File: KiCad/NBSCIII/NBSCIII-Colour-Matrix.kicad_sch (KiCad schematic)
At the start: 24 parts, among them U9 LM324

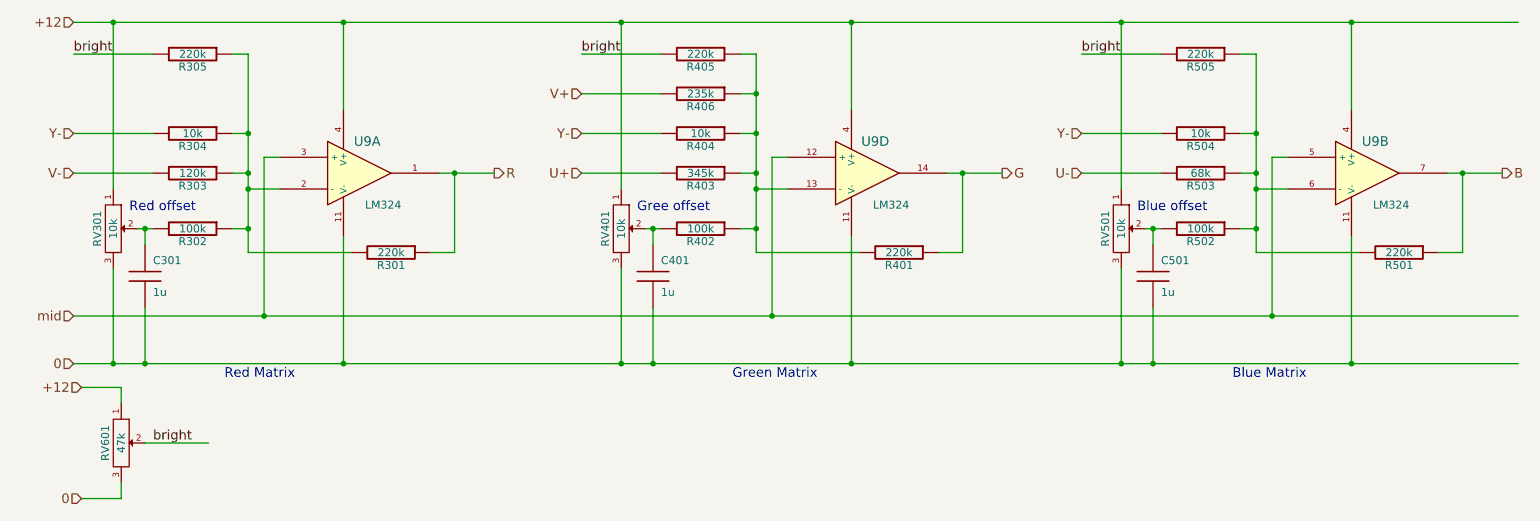
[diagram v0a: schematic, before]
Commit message: unrescue to Device:C
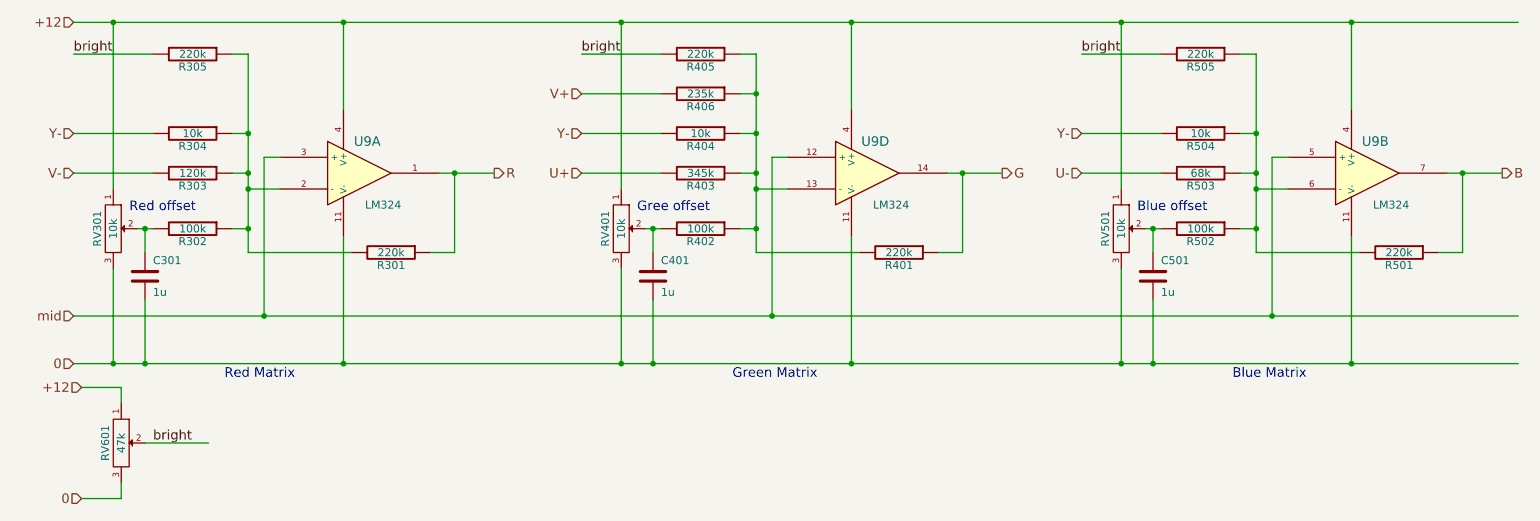
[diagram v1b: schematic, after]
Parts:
- C301, C401, C501: symbol NBSCIII-rescue:C -> Device:C
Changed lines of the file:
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@@
     (stroke (width 0) (type default) (color 0 0 0 0))
   )
-  (wire (pts (xy 123.19 82.55) (xy 123.19 91.44))
+  (wire (pts (xy 123.19 81.28) (xy 123.19 91.44))
     (stroke (width 0) (type default) (color 0 0 0 0))
   )
@@
     (stroke (width 0) (type default) (color 0 0 0 0))
   )
-  (wire (pts (xy 41.91 69.85) (xy 41.91 72.39))
+  (wire (pts (xy 41.91 69.85) (xy 41.91 73.66))
     (stroke (width 0) (type default) (color 0 0 0 0))
   )
@@
     (stroke (width 0) (type default) (color 0 0 0 0))
   )
-  (wire (pts (xy 203.2 69.85) (xy 203.2 72.39))
+  (wire (pts (xy 203.2 69.85) (xy 203.2 73.66))
     (stroke (width 0) (type default) (color 0 0 0 0))
   )
@@
     (stroke (width 0) (type default) (color 0 0 0 0))
   )
-  (wire (pts (xy 203.2 82.55) (xy 203.2 91.44))
-    (stroke (width 0) (type default) (color 0 0 0 0))
-  )
-  (wire (pts (xy 123.19 69.85) (xy 123.19 72.39))
+  (wire (pts (xy 203.2 81.28) (xy 203.2 91.44))
     (stroke (width 0) (type default) (color 0 0 0 0))
   )
@@
     (stroke (width 0) (type default) (color 0 0 0 0))
   )
+  (wire (pts (xy 123.19 69.85) (xy 123.19 73.66))
+    (stroke (width 0) (type default) (color 0 0 0 0))
+  )
   (wire (pts (xy 203.2 91.44) (xy 198.12 91.44))
     (stroke (width 0) (type default) (color 0 0 0 0))
@@
     (stroke (width 0) (type default) (color 0 0 0 0))
   )
-  (wire (pts (xy 41.91 82.55) (xy 41.91 91.44))
+  (wire (pts (xy 41.91 81.28) (xy 41.91 91.44))
     (stroke (width 0) (type default) (color 0 0 0 0))
   )
@@
     (pin "3")
   )
-  (symbol (lib_id "NBSCIII-rescue:C") (at 41.91 77.47 0) (unit 1)
+  (symbol (lib_id "Device:C") (at 41.91 77.47 0) (unit 1)
     (in_bom yes) (on_board yes)
     (property "Reference" "C301" (id 0) (at 43.18 74.93 0)
@@
     (pin "3")
   )
-  (symbol (lib_id "NBSCIII-rescue:C") (at 123.19 77.47 0) (unit 1)
+  (symbol (lib_id "Device:C") (at 123.19 77.47 0) (unit 1)
     (in_bom yes) (on_board yes)
     (property "Reference" "C401" (id 0) (at 124.46 74.93 0)
@@
     (pin "3")
   )
-  (symbol (lib_id "NBSCIII-rescue:C") (at 203.2 77.47 0) (unit 1)
+  (symbol (lib_id "Device:C") (at 203.2 77.47 0) (unit 1)
     (in_bom yes) (on_board yes)
     (property "Reference" "C501" (id 0) (at 204.47 74.93 0)

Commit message: unrescue Device:R
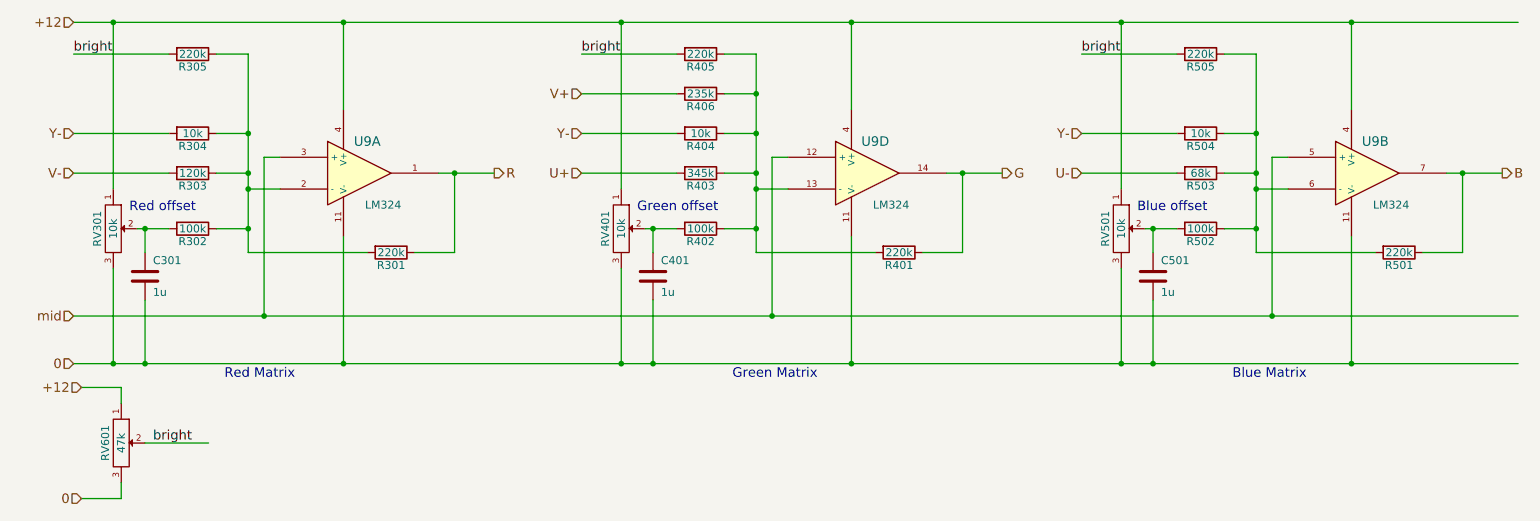
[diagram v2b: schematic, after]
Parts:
- R301, R302, R303, R304, R305, R401, R402, R403, R404, R405, R406, R501, R502, R503, R504, R505: symbol NBSCIII-rescue:R -> Device:R
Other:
- note added: "Green offset"
- note removed: "Gree offset"

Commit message: unrescue Device:R_potentiometer
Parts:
- RV301, RV401, RV501, RV601: symbol NBSCIII-rescue:POT -> Device:R_Potentiometer
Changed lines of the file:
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@@
     (stroke (width 0) (type default) (color 0 0 0 0))
   )
-  (wire (pts (xy 198.12 63.5) (xy 198.12 36.83))
+  (wire (pts (xy 198.12 36.83) (xy 198.12 66.04))
     (stroke (width 0) (type default) (color 0 0 0 0))
   )
@@
     (stroke (width 0) (type default) (color 0 0 0 0))
   )
-  (wire (pts (xy 36.83 76.2) (xy 36.83 91.44))
+  (wire (pts (xy 36.83 73.66) (xy 36.83 91.44))
     (stroke (width 0) (type default) (color 0 0 0 0))
   )
@@
     (stroke (width 0) (type default) (color 0 0 0 0))
   )
-  (wire (pts (xy 198.12 76.2) (xy 198.12 91.44))
+  (wire (pts (xy 198.12 73.66) (xy 198.12 91.44))
+    (stroke (width 0) (type default) (color 0 0 0 0))
+  )
+  (wire (pts (xy 118.11 73.66) (xy 118.11 91.44))
     (stroke (width 0) (type default) (color 0 0 0 0))
   )
@@
     (stroke (width 0) (type default) (color 0 0 0 0))
   )
-  (wire (pts (xy 38.1 113.03) (xy 38.1 110.49))
+  (wire (pts (xy 38.1 107.95) (xy 38.1 113.03))
     (stroke (width 0) (type default) (color 0 0 0 0))
   )
@@
     (stroke (width 0) (type default) (color 0 0 0 0))
   )
-  (wire (pts (xy 118.11 63.5) (xy 118.11 36.83))
+  (wire (pts (xy 118.11 36.83) (xy 118.11 66.04))
     (stroke (width 0) (type default) (color 0 0 0 0))
   )
@@
     (stroke (width 0) (type default) (color 0 0 0 0))
   )
-  (wire (pts (xy 36.83 63.5) (xy 36.83 36.83))
+  (wire (pts (xy 36.83 36.83) (xy 36.83 66.04))
     (stroke (width 0) (type default) (color 0 0 0 0))
   )
@@
     (stroke (width 0) (type default) (color 0 0 0 0))
   )
-  (wire (pts (xy 118.11 76.2) (xy 118.11 91.44))
-    (stroke (width 0) (type default) (color 0 0 0 0))
-  )
   (wire (pts (xy 41.91 91.44) (xy 36.83 91.44))
     (stroke (width 0) (type default) (color 0 0 0 0))
@@
     (stroke (width 0) (type default) (color 0 0 0 0))
   )
-  (wire (pts (xy 38.1 97.79) (xy 38.1 95.25))
+  (wire (pts (xy 38.1 95.25) (xy 38.1 100.33))
     (stroke (width 0) (type default) (color 0 0 0 0))
   )
@@
     (effects (font (size 1.524 1.524)) (justify left bottom))
   )
-  (text "Green offset" (at 120.65 67.31 0)
+  (text "Green offset" (at 120.65 67.31 90)
     (effects (font (size 1.524 1.524)) (justify left bottom))
   )
@@
     (pin "2")
   )
-  (symbol (lib_id "NBSCIII-rescue:POT") (at 36.83 69.85 270) (unit 1)
-    (in_bom yes) (on_board yes)
-    (property "Reference" "RV301" (id 0) (at 34.29 69.85 0))
-    (property "Value" "10k" (id 1) (at 36.83 69.85 0))
+  (symbol (lib_id "Device:R_Potentiometer") (at 36.83 69.85 0) (unit 1)
+    (in_bom yes) (on_board yes)
+    (property "Reference" "RV301" (id 0) (at 31.75 74.93 0))
+    (property "Value" "10k" (id 1) (at 36.83 69.85 90))
     (property "Footprint" "" (id 2) (at 36.83 69.85 0)
       (effects (font (size 1.27 1.27)) hide)
@@
     (pin "2")
   )
-  (symbol (lib_id "NBSCIII-rescue:POT") (at 118.11 69.85 270) (unit 1)
-    (in_bom yes) (on_board yes)
-    (property "Reference" "RV401" (id 0) (at 115.57 69.85 0))
-    (property "Value" "10k" (id 1) (at 118.11 69.85 0))
+  (symbol (lib_id "Device:R_Potentiometer") (at 118.11 69.85 0) (unit 1)
+    (in_bom yes) (on_board yes)
+    (property "Reference" "RV401" (id 0) (at 113.03 72.39 0))
+    (property "Value" "10k" (id 1) (at 118.11 69.85 90))
     (property "Footprint" "" (id 2) (at 118.11 69.85 0)
       (effects (font (size 1.27 1.27)) hide)
@@
     (pin "2")
   )
-  (symbol (lib_id "NBSCIII-rescue:POT") (at 198.12 69.85 270) (unit 1)
-    (in_bom yes) (on_board yes)
-    (property "Reference" "RV501" (id 0) (at 195.58 69.85 0))
-    (property "Value" "10k" (id 1) (at 198.12 69.85 0))
+  (symbol (lib_id "Device:R_Potentiometer") (at 198.12 69.85 0) (unit 1)
+    (in_bom yes) (on_board yes)
+    (property "Reference" "RV501" (id 0) (at 193.04 73.66 0))
+    (property "Value" "10k" (id 1) (at 198.12 69.85 90))
     (property "Footprint" "" (id 2) (at 198.12 69.85 0)
       (effects (font (size 1.27 1.27)) hide)
@@
     (pin "2")
   )
-  (symbol (lib_id "NBSCIII-rescue:POT") (at 38.1 104.14 270) (unit 1)
-    (in_bom yes) (on_board yes)
-    (property "Reference" "RV601" (id 0) (at 35.56 104.14 0))
-    (property "Value" "47k" (id 1) (at 38.1 104.14 0))
+  (symbol (lib_id "Device:R_Potentiometer") (at 38.1 104.14 0) (unit 1)
+    (in_bom yes) (on_board yes)
+    (property "Reference" "RV601" (id 0) (at 33.02 106.68 0))
+    (property "Value" "47k" (id 1) (at 38.1 104.14 90))
     (property "Footprint" "" (id 2) (at 38.1 104.14 0)
       (effects (font (size 1.27 1.27)) hide)

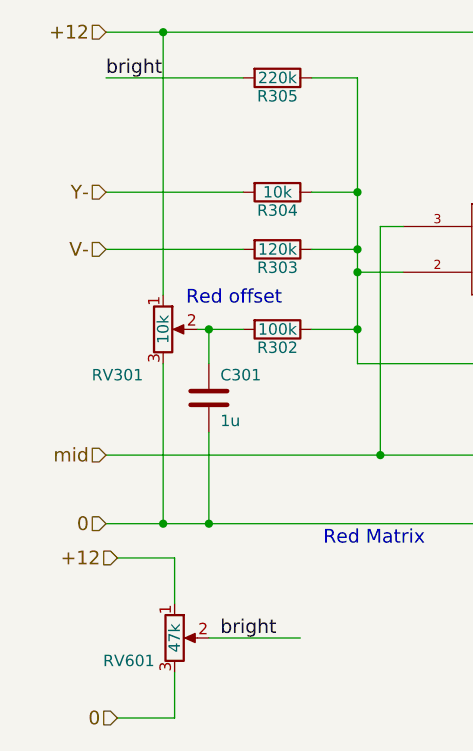
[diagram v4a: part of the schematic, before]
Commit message: Simplify power distribution and make global
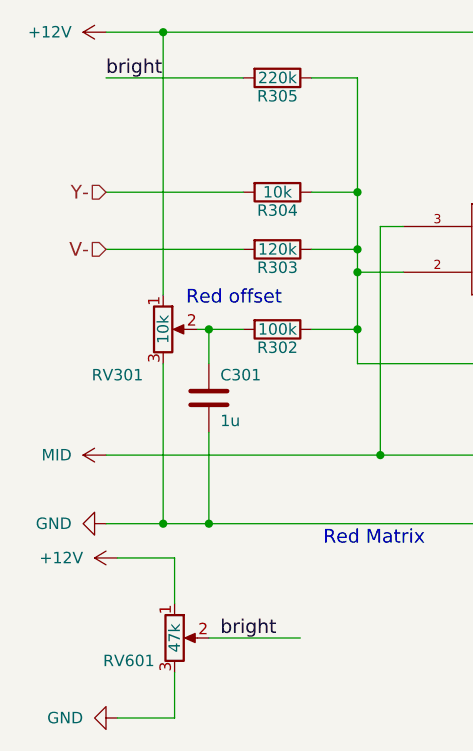
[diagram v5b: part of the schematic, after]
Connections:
- net +12 renamed +12V
- net 0 renamed GND
- net mid renamed MID
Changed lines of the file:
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@@
-    (effects (font (size 1.524 1.524)) (justify right))
-  )
-  (hierarchical_label "+12" (shape input) (at 30.48 36.83 180)
     (effects (font (size 1.524 1.524)) (justify right))
   )
@@
     (effects (font (size 1.524 1.524)) (justify right))
   )
-  (hierarchical_label "mid" (shape input) (at 30.48 83.82 180)
-    (effects (font (size 1.524 1.524)) (justify right))
-  )
   (hierarchical_label "R" (shape output) (at 97.79 60.96 0)
     (effects (font (size 1.524 1.524)) (justify left))
   )
-  (hierarchical_label "0" (shape input) (at 31.75 113.03 180)
-    (effects (font (size 1.524 1.524)) (justify right))
-  )
   (hierarchical_label "V-" (shape input) (at 30.48 60.96 180)
-    (effects (font (size 1.524 1.524)) (justify right))
-  )
-  (hierarchical_label "0" (shape input) (at 30.48 91.44 180)
-    (effects (font (size 1.524 1.524)) (justify right))
-  )
-  (hierarchical_label "+12" (shape input) (at 31.75 95.25 180)
     (effects (font (size 1.524 1.524)) (justify right))
   )
@@
     (pin "3")
   )
+  (symbol (lib_id "power:+12V") (at 30.48 36.83 90) (unit 1)
+    (in_bom yes) (on_board yes) (fields_autoplaced)
+    (property "Reference" "#PWR0113" (id 0) (at 34.29 36.83 0)
+      (effects (font (size 1.27 1.27)) hide)
+    )
+    (property "Value" "+12V" (id 1) (at 26.67 36.8299 90)
+      (effects (font (size 1.27 1.27)) (justify left))
+    )
+    (property "Footprint" "" (id 2) (at 30.48 36.83 0)
+      (effects (font (size 1.27 1.27)) hide)
+    )
+    (property "Datasheet" "" (id 3) (at 30.48 36.83 0)
+      (effects (font (size 1.27 1.27)) hide)
+    )
+    (pin "1")
+  )
+  (symbol (lib_id "power:GND") (at 31.75 113.03 270) (unit 1)
+    (in_bom yes) (on_board yes) (fields_autoplaced)
+    (property "Reference" "#PWR0117" (id 0) (at 25.4 113.03 0)
+      (effects (font (size 1.27 1.27)) hide)
+    )
+    (property "Value" "GND" (id 1) (at 27.94 113.0299 90)
+      (effects (font (size 1.27 1.27)) (justify right))
+    )
+    (property "Footprint" "" (id 2) (at 31.75 113.03 0)
+      (effects (font (size 1.27 1.27)) hide)
+    )
+    (property "Datasheet" "" (id 3) (at 31.75 113.03 0)
+      (effects (font (size 1.27 1.27)) hide)
+    )
+    (pin "1")
+  )
+  (symbol (lib_id "NBSCIII:MID") (at 30.48 83.82 90) (unit 1)
+    (in_bom yes) (on_board yes) (fields_autoplaced)
+    (property "Reference" "#PWR0116" (id 0) (at 34.29 83.82 0)
+      (effects (font (size 1.27 1.27)) hide)
+    )
+    (property "Value" "MID" (id 1) (at 26.67 83.8199 90)
+      (effects (font (size 1.27 1.27)) (justify left))
+    )
+    (property "Footprint" "" (id 2) (at 30.48 83.82 0)
+      (effects (font (size 1.27 1.27)) hide)
+    )
+    (property "Datasheet" "" (id 3) (at 30.48 83.82 0)
+      (effects (font (size 1.27 1.27)) hide)
+    )
+    (pin "1")
+  )
+  (symbol (lib_id "power:+12V") (at 31.75 95.25 90) (unit 1)
+    (in_bom yes) (on_board yes) (fields_autoplaced)
+    (property "Reference" "#PWR0115" (id 0) (at 35.56 95.25 0)
+      (effects (font (size 1.27 1.27)) hide)
+    )
+    (property "Value" "+12V" (id 1) (at 27.94 95.2499 90)
+      (effects (font (size 1.27 1.27)) (justify left))
+    )
+    (property "Footprint" "" (id 2) (at 31.75 95.25 0)
+      (effects (font (size 1.27 1.27)) hide)
+    )
+    (property "Datasheet" "" (id 3) (at 31.75 95.25 0)
+      (effects (font (size 1.27 1.27)) hide)
+    )
+    (pin "1")
+  )
+  (symbol (lib_id "power:GND") (at 30.48 91.44 270) (unit 1)
+    (in_bom yes) (on_board yes) (fields_autoplaced)
+    (property "Reference" "#PWR0114" (id 0) (at 24.13 91.44 0)
+      (effects (font (size 1.27 1.27)) hide)
+    )
+    (property "Value" "GND" (id 1) (at 26.67 91.4399 90)
+      (effects (font (size 1.27 1.27)) (justify right))
+    )
+    (property "Footprint" "" (id 2) (at 30.48 91.44 0)
+      (effects (font (size 1.27 1.27)) hide)
+    )
+    (property "Datasheet" "" (id 3) (at 30.48 91.44 0)
+      (effects (font (size 1.27 1.27)) hide)
+    )
+    (pin "1")
+  )
 )
